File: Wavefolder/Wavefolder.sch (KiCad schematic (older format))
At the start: 43 parts, among them J1 Clock, J2 EuroPower, J3 SSD1306, J4 CV, J5 Gate, Q1 BC547, Q2 BC557, SW1 Reset, U1 TL082, U2 L7805, U3 PIC18F26Q43

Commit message: Wavefolder, will it fits ?
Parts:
- removed C3: 10u, Capacitor_THT:CP_Radial_D8.0mm_P3.80mm, symbol Device:CP
- removed C4: 1u, Capacitor_THT:CP_Radial_D8.0mm_P3.80mm, symbol Device:CP
- removed C5: 100n, Capacitor_THT:C_Disc_D7.0mm_W2.5mm_P5.00mm, symbol Device:C
- removed C6: 10n, Capacitor_THT:C_Disc_D7.0mm_W2.5mm_P5.00mm, symbol Device:C
- removed D1, D2, D4, D5: LED, LED_SMD:LED_1206_3216Metric_Castellated, symbol Device:LED
- removed H3, H4: Mounting_Holes, Kosmo_panel:Kosmo_Panel_Dual_Mounting_Holes, symbol Kosmo:Mounting_Holes
- removed J3: SSD1306, telec:SSD1306_096in_I2C, symbol Connector:Conn_01x05_Female
- removed RV3: R_POT_TRIM, Potentiometer_THT:Potentiometer_Bourns_3299W_Vertical, symbol Device:R_POT_TRIM
- removed SW1: Reset, Button_Switch_THT:SW_PUSH_6mm, symbol Switch:SW_SPST
- removed U2: L7805, Package_TO_SOT_THT:TO-220-3_Horizontal_TabDown, symbol Regulator_Linear:L7805
- removed U3: PIC18F26Q43, Package_SO:SOIC-28W_7.5x17.9mm_P1.27mm, symbol telec:PIC18F26Q43
- added J3: Sig2, telec:JackHole, symbol Connector:AudioJack3_Switch
- added J6: CV2, telec:JackHole, symbol Connector:AudioJack3_Switch
- added Q3, Q5: BC557, Package_TO_SOT_THT:TO-92_Inline_Wide, symbol Transistor_BJT:BC557
- added Q4, Q6: BC547, Package_TO_SOT_THT:TO-92_Inline_Wide, symbol Transistor_BJT:BC547
- added R13, R14: 10k, Resistor_THT:R_Axial_DIN0204_L3.6mm_D1.6mm_P7.62mm_Horizontal, symbol Device:R
- added RV3: 100k, Potentiometer_THT:Potentiometer_Alps_RK09K_Single_Vertical, symbol Device:R_POT
- added U1, U3: TL074, Package_DIP:DIP-14_W7.62mm_LongPads, symbol Amplifier_Operational:TL074
- J1: value Clock -> Sig1
- J4: value CV -> Out1
- J5: value Gate -> Out2
- LOGO1: footprint logo:telec-32 -> logo:telec-8
- R1: value 100k -> 15k
- R11, R12: value 1k -> 15k
- R2, R6: value 10k -> 15k
- R4: value 1k -> 47k; footprint Resistor_SMD:R_1206_3216Metric_Pad1.42x1.75mm_HandSolder -> Resistor_THT:R_Axial_DIN0204_L3.6mm_D1.6mm_P7.62mm_Horizontal
- R5: value 1k -> 15k; footprint Resistor_SMD:R_1206_3216Metric_Pad1.42x1.75mm_HandSolder -> Resistor_THT:R_Axial_DIN0204_L3.6mm_D1.6mm_P7.62mm_Horizontal
- R7: value 1k -> 2k2; footprint Resistor_SMD:R_1206_3216Metric_Pad1.42x1.75mm_HandSolder -> Resistor_THT:R_Axial_DIN0204_L3.6mm_D1.6mm_P7.62mm_Horizontal
- R8: value 1k -> 15K; footprint Resistor_SMD:R_1206_3216Metric_Pad1.42x1.75mm_HandSolder -> Resistor_THT:R_Axial_DIN0204_L3.6mm_D1.6mm_P7.62mm_Horizontal
- R9: value 10k -> 6k8
- RV1: value R_POT_Small -> 100k; footprint Potentiometer_THT:Potentiometer_Bourns_3339P_Vertical -> Potentiometer_THT:Potentiometer_Alps_RK09K_Single_Vertical; symbol Device:R_POT_Small -> Device:R_POT
- RV2: value R_POT -> 100k; footprint Potentiometer_THT:Potentiometer_Piher_T-16L_Single_Vertical_Hole -> Potentiometer_THT:Potentiometer_Alps_RK09K_Single_Vertical
- renumbered U1 to U2
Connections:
- net labels added: CV2, Out1, Sig1, Sig2
- net labels removed: +5V, Rst, SCL, SDA
- wire segments 59 -> 69
- no-connect marks 11 -> 17
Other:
- note added: "This part from Adamski A."
- note added: "This part from organfairy"
- note added: "x -1"
- note added: "x -4.7"
- note added: "x -6.8"
- note removed: "Output buffer"
- moved on the sheet: C1, C2, D3, J1, Q1, Q2, R1, U2A, U2B, U2C

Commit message: Wavefolder layout
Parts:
- removed D6: LED, LED_SMD:LED_1206_3216Metric_ReverseMount_Hole1.8x2.4mm, symbol Device:LED
- removed R10: 1k, Resistor_SMD:R_1206_3216Metric_Pad1.42x1.75mm_HandSolder, symbol Device:R
- added D1, D2, D4: 1N4148, Diode_THT:D_DO-35_SOD27_P7.62mm_Horizontal, symbol Diode:1N4148
- added R15, R16, R26, R27, R28, R29: 100k, Resistor_SMD:R_1206_3216Metric_Pad1.42x1.75mm_HandSolder, symbol Device:R
- added R17, R18, R19, R20, R22: 100k, Resistor_THT:R_Axial_DIN0204_L3.6mm_D1.6mm_P7.62mm_Horizontal, symbol Device:R
- added R21: 100k, Resistor_THT:R_Axial_DIN0204_L3.6mm_D1.6mm_P2.54mm_Vertical, symbol Device:R
- added R23, R24: 15k, Resistor_THT:R_Axial_DIN0204_L3.6mm_D1.6mm_P7.62mm_Horizontal, symbol Device:R
- added R25: 1k, Resistor_SMD:R_1206_3216Metric_Pad1.42x1.75mm_HandSolder, symbol Device:R
- added unit 1 of U1
- added unit 1 of U3
- added unit 4 of U3
- added unit 3 of U3
- added unit 5 of U3
- added U4: TL082, Package_SO:SOIC-8_3.9x4.9mm_P1.27mm, symbol Amplifier_Operational:TL082
- R1, R11, R12, R13, R14, R2, R4, R5, R6, R7, R8, R9: footprint Resistor_THT:R_Axial_DIN0204_L3.6mm_D1.6mm_P7.62mm_Horizontal -> Resistor_THT:R_Axial_DIN0204_L3.6mm_D1.6mm_P2.54mm_Vertical
- U2: footprint Package_DIP:DIP-8_W7.62mm_LongPads -> Package_SO:SOIC-8_3.9x4.9mm_P1.27mm
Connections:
- net +12V: now also RV3.1, R24.2, U3.4 (V+), U4.8 (V+)
- net -12V: now also RV3.3, R23.1, U3.11 (V-), U4.4 (V-)
- net CV2: now also R26.1
- net GND: now also U2.5 (+), U3.3 (+), U4.5 (+)
- net Out1: now also R14.1; no longer R14.2
- net Sig2: now also R15.1
- net at RV1.2: now also U1.3 (+)
- net at D3.1 (K): now also U3.5 (+), D1.1 (K), R23.2
- net ~Sig2: now reaches D3.2 (A)
- net ~Sig2: now also R16.2, R17.1, R18.1, U4.7
- net at J5.T: now also R25.2, U4.2 (-)
- net Offset: now reaches U2.1
- net Offset: now also R19.1, R29.2, U3.10 (+)
- net at U2.2 (-): now also R28.2, R29.1
- net at U2.3 (+): now also RV3.2
- net at U2.6 (-): now also RV2.2, RV2.3, R26.2
- net at U2.7: now also R27.2, R28.1
- net at Q1.2 (B), Q2.2 (B): now also U1.1, U1.2 (-)
- net at R9.1, U1.8: now also R8.1; no longer R8.2
- net at R7.2, U1.9 (-): now also R8.2; no longer R8.1
- net at Q5.1 (C), Q6.1 (C): now also R13.2; no longer R13.1
- net at RV2.1: now also R27.1
- net at U3.6 (-): now also U3.7, D2.1 (K)
- new net: R13.1, R14.2, U1.13 (-)
- new net: R19.2, R22.1, U3.2 (-)
- new net: R18.2, R21.1, U3.13 (-)
- new net: R17.2, R20.1, U3.9 (-)
- new net: R25.1, U4.1
- new net: R15.2, R16.1, U4.6 (-)
- new net Bottom: D1.2 (A), R21.2, U3.14
- new net Out2: D2.2 (A), D4.2 (A), R24.1, U4.3 (+)
- new net Top: D4.1 (K), R20.2, U3.8
- new net ~Offset: R22.2, U3.1, U3.12 (+)
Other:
- note added: "This part is from Adamski A."
- note added: "This part is from organfairy"
- note removed: "Front Panel"
- note removed: "This part from Adamski A."
- note removed: "This part from organfairy"
- moved on the sheet: C1, C2, D3, H1, H2, J1, J2, J3, J4, J5, J6, Q1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

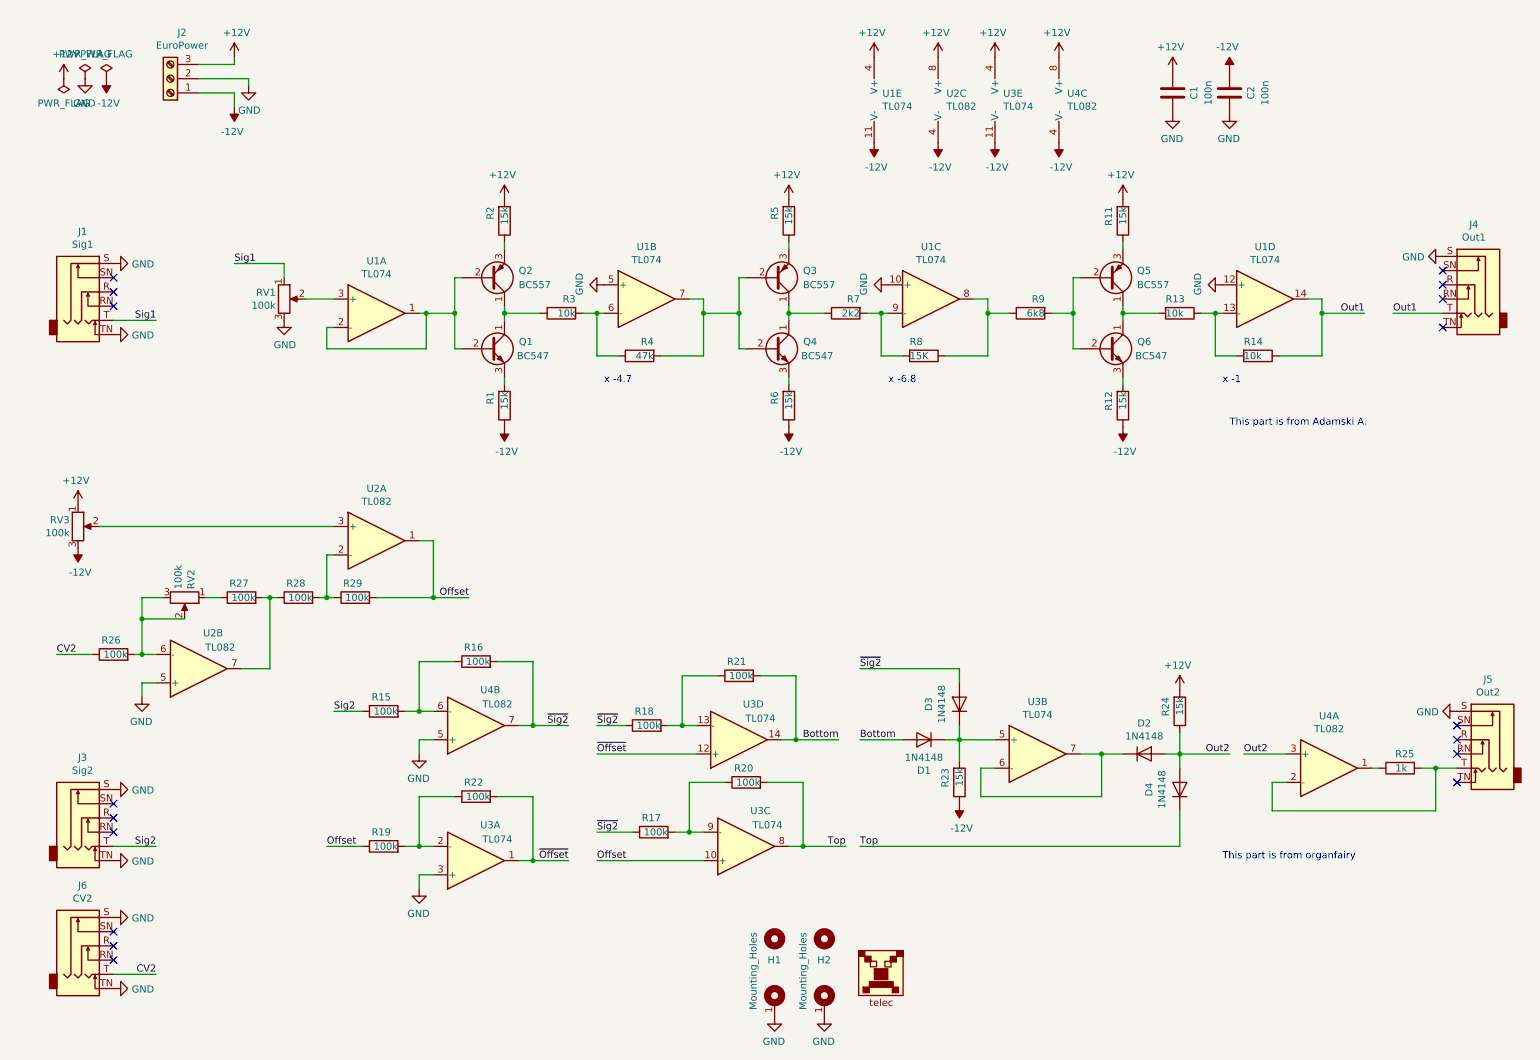
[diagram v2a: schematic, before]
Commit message: Wavefolder design
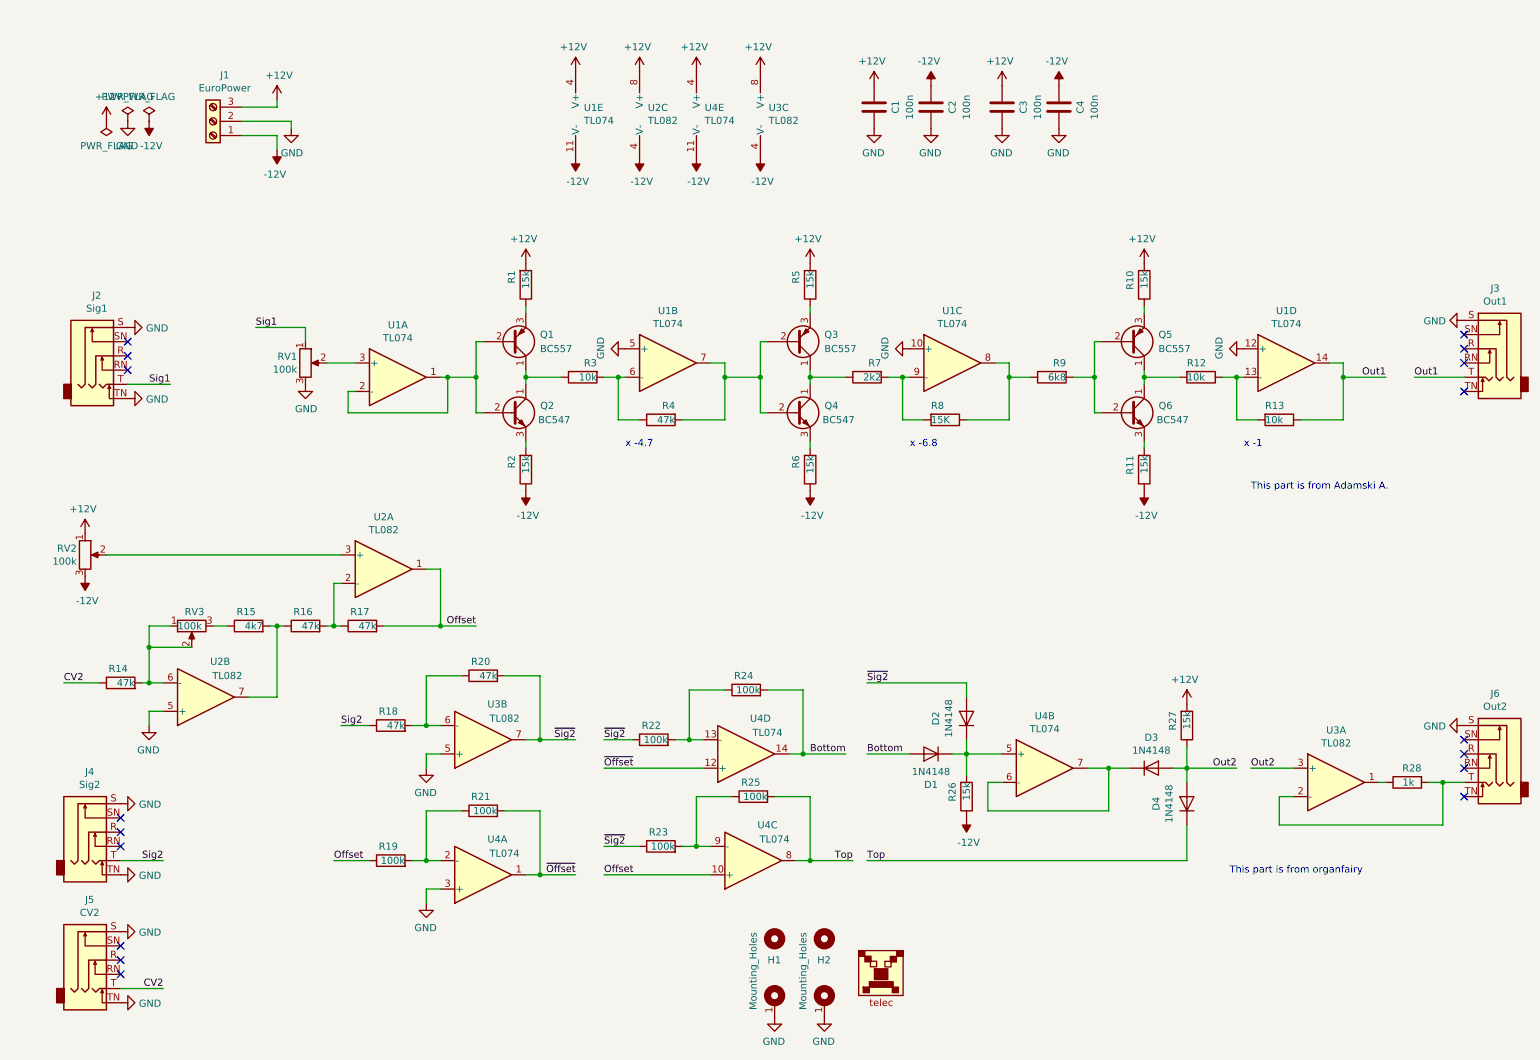
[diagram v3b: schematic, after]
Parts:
- added C3, C4: 100n, Capacitor_SMD:C_1206_3216Metric, symbol Device:C
- C1, C2: footprint Capacitor_THT:C_Disc_D7.0mm_W2.5mm_P5.00mm -> Capacitor_SMD:C_1206_3216Metric
- R14: renamed from R26; value 100k -> 47k
- R15: renamed from R27; value 100k -> 4k7
- R16: renamed from R28; value 100k -> 47k
- R17: renamed from R29; value 100k -> 47k
- R18: renamed from R15; value 100k -> 47k
- R20: renamed from R16; value 100k -> 47k
- renumbered D3 to D2, D2 to D3, J2 to J1, J1 to J2, J4 to J3, J3 to J4, J6 to J5, J5 to J6, Q2 to Q1, Q1 to Q2, R2 to R1, R11 to R10, R12 to R11, R13 to R12, R14 to R13, R1 to R2, R22 to R21, R18 to R22, R17 to R23, R21 to R24, R20 to R25, R23 to R26, R24 to R27, R25 to R28, RV3 to RV2, RV2 to RV3, U4 to U3, U3 to U4
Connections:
- net +12V: now also C3.2
- net -12V: now also C4.2
- net GND: now also C3.1, C4.1
- net at RV3.1: now also R14.2, RV3.2, U2.6 (-); no longer R15.1
- new net: R15.1, RV3.3
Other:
- moved on the sheet: C1, C2, D1, D2, D3, D4, J1, J2, J3, J4, J5, J6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

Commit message: Wavefolder done !
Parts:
- U2, U3: footprint Package_DIP:DIP-8_W7.62mm_LongPads -> Package_SO:SOIC-8_3.9x4.9mm_P1.27mm
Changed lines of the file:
@@
 F 0 "U2" H 4908 1196 50  0000 L CNN
 F 1 "TL082" H 4908 1105 50  0000 L CNN
-F 2 "Package_DIP:DIP-8_W7.62mm_LongPads" H 4950 1150 50  0001 C CNN
+F 2 "Package_SO:SOIC-8_3.9x4.9mm_P1.27mm" H 4950 1150 50  0001 C CNN
 F 3 "http://www.ti.com/lit/ds/symlink/tl081.pdf" H 4950 1150 50  0001 C CNN
 	3    4950 1150
@@
 F 0 "U3" H 5758 1196 50  0000 L CNN
 F 1 "TL082" H 5758 1105 50  0000 L CNN
-F 2 "Package_DIP:DIP-8_W7.62mm_LongPads" H 5800 1150 50  0001 C CNN
+F 2 "Package_SO:SOIC-8_3.9x4.9mm_P1.27mm" H 5800 1150 50  0001 C CNN
 F 3 "http://www.ti.com/lit/ds/symlink/tl081.pdf" H 5800 1150 50  0001 C CNN
 	3    5800 1150

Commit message: Wavefolder done and tested!
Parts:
- added R13.1: 1k, Resistor_THT:R_Axial_DIN0204_L3.6mm_D1.6mm_P2.54mm_Vertical, symbol Device:R
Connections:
- net Out1: now also R13.1.1; no longer J3.T
- new net: J3.T, R13.1.2
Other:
- moved on the sheet: Q1, Q2, Q3, Q4, Q5, Q6, R1, R10, R11, R12, R13, R2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

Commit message: updated footprints on Wavefolder
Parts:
- J2, J3, J4, J5, J6: footprint telec:JackHole -> telec:Jack_Hole_Square; symbol Connector:AudioJack3_Switch -> Connector:AudioJack3_SwitchTR
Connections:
- no-connect marks 17 -> 12
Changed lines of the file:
@@
 $EndComp
 $Comp
-L Connector:AudioJack3_Switch J2
+L Connector:AudioJack3_SwitchTR J2
 U 1 1 5F0BD040
 P 1050 2850
 F 0 "J2" H 1032 3275 50  0000 C CNN
 F 1 "Sig1" H 1032 3184 50  0000 C CNN
-F 2 "telec:JackHole" H 1050 2850 50  0001 C CNN
+F 2 "telec:Jack_Hole_Square" H 1050 2850 50  0001 C CNN
 F 3 "~" H 1050 2850 50  0001 C CNN
 	1    1050 2850
@@
 	2300 1300 2300 1400
 $Comp
-L Connector:AudioJack3_Switch J6
+L Connector:AudioJack3_SwitchTR J6
 U 1 1 5F41F070
 P 10850 5650
 F 0 "J6" H 10832 6075 50  0000 C CNN
 F 1 "Out2" H 10832 5984 50  0000 C CNN
-F 2 "telec:JackHole" H 10850 5650 50  0001 C CNN
+F 2 "telec:Jack_Hole_Square" H 10850 5650 50  0001 C CNN
 F 3 "~" H 10850 5650 50  0001 C CNN
 	1    10850 5650
@@
 $EndComp
 $Comp
-L Connector:AudioJack3_Switch J3
+L Connector:AudioJack3_SwitchTR J3
 U 1 1 5F4208DD
 P 10850 2800
 F 0 "J3" H 10832 3225 50  0000 C CNN
 F 1 "Out1" H 10832 3134 50  0000 C CNN
-F 2 "telec:JackHole" H 10850 2800 50  0001 C CNN
+F 2 "telec:Jack_Hole_Square" H 10850 2800 50  0001 C CNN
 F 3 "~" H 10850 2800 50  0001 C CNN
 	1    10850 2800
@@
 NoConn ~ 10650 5750
 NoConn ~ 10650 5650
-NoConn ~ 10650 5550
 NoConn ~ 10650 5950
 $Comp
 L power:GND #PWR033
 U 1 1 5F62E5EC
-P 10650 5450
-F 0 "#PWR033" H 10650 5200 50  0001 C CNN
-F 1 "GND" V 10655 5322 50  0000 R CNN
-F 2 "" H 10650 5450 50  0001 C CNN
-F 3 "" H 10650 5450 50  0001 C CNN
-	1    10650 5450
+P 10650 5550
+F 0 "#PWR033" H 10650 5300 50  0001 C CNN
+F 1 "GND" V 10655 5422 50  0000 R CNN
+F 2 "" H 10650 5550 50  0001 C CNN
+F 3 "" H 10650 5550 50  0001 C CNN
+	1    10650 5550
 	0    1    1    0
 $EndComp
 NoConn ~ 10650 2900
 NoConn ~ 10650 2800
-NoConn ~ 10650 2700
 NoConn ~ 10650 3100
 $Comp
 L power:GND #PWR019
 U 1 1 5F62EF49
-P 10650 2600
-F 0 "#PWR019" H 10650 2350 50  0001 C CNN
-F 1 "GND" V 10655 2472 50  0000 R CNN
-F 2 "" H 10650 2600 50  0001 C CNN
-F 3 "" H 10650 2600 50  0001 C CNN
-	1    10650 2600
+P 10650 2700
+F 0 "#PWR019" H 10650 2450 50  0001 C CNN
+F 1 "GND" V 10655 2572 50  0000 R CNN
+F 2 "" H 10650 2700 50  0001 C CNN
+F 3 "" H 10650 2700 50  0001 C CNN
+	1    10650 2700
 	0    1    1    0
 $EndComp
 NoConn ~ 1250 2950
 NoConn ~ 1250 2850
-NoConn ~ 1250 2750
 $Comp
 L power:GND #PWR07
 U 1 1 5F63005B
-P 1250 2650
-F 0 "#PWR07" H 1250 2400 50  0001 C CNN
-F 1 "GND" V 1255 2522 50  0000 R CNN
-F 2 "" H 1250 2650 50  0001 C CNN
-F 3 "" H 1250 2650 50  0001 C CNN
-	1    1250 2650
+P 1250 2750
+F 0 "#PWR07" H 1250 2500 50  0001 C CNN
+F 1 "GND" V 1255 2622 50  0000 R CNN
+F 2 "" H 1250 2750 50  0001 C CNN
+F 3 "" H 1250 2750 50  0001 C CNN
+	1    1250 2750
 	0    -1   1    0
 $EndComp
@@
 Sig1
 $Comp
-L Connector:AudioJack3_Switch J4
+L Connector:AudioJack3_SwitchTR J4
 U 1 1 6449AD27
 P 1000 6200
 F 0 "J4" H 982 6625 50  0000 C CNN
 F 1 "Sig2" H 982 6534 50  0000 C CNN
-F 2 "telec:JackHole" H 1000 6200 50  0001 C CNN
+F 2 "telec:Jack_Hole_Square" H 1000 6200 50  0001 C CNN
 F 3 "~" H 1000 6200 50  0001 C CNN
 	1    1000 6200
@@
 NoConn ~ 1200 6300
 NoConn ~ 1200 6200
-NoConn ~ 1200 6100
 $Comp
 L power:GND #PWR022
 U 1 1 6449AD30
-P 1200 6000
-F 0 "#PWR022" H 1200 5750 50  0001 C CNN
-F 1 "GND" V 1205 5872 50  0000 R CNN
-F 2 "" H 1200 6000 50  0001 C CNN
-F 3 "" H 1200 6000 50  0001 C CNN
-	1    1200 6000
+P 1200 6100
+F 0 "#PWR022" H 1200 5850 50  0001 C CNN
+F 1 "GND" V 1205 5972 50  0000 R CNN
+F 2 "" H 1200 6100 50  0001 C CNN
+F 3 "" H 1200 6100 50  0001 C CNN
+	1    1200 6100
 	0    -1   1    0
 $EndComp
@@
 Sig2
 $Comp
-L Connector:AudioJack3_Switch J5
+L Connector:AudioJack3_SwitchTR J5
 U 1 1 6449C304
 P 1000 7100
 F 0 "J5" H 982 7525 50  0000 C CNN
 F 1 "CV2" H 982 7434 50  0000 C CNN
-F 2 "telec:JackHole" H 1000 7100 50  0001 C CNN
+F 2 "telec:Jack_Hole_Square" H 1000 7100 50  0001 C CNN
 F 3 "~" H 1000 7100 50  0001 C CNN
 	1    1000 7100
@@
 NoConn ~ 1200 7200
 NoConn ~ 1200 7100
-NoConn ~ 1200 7000
 $Comp
 L power:GND #PWR024
 U 1 1 6449C30D
-P 1200 6900
-F 0 "#PWR024" H 1200 6650 50  0001 C CNN
-F 1 "GND" V 1205 6772 50  0000 R CNN
-F 2 "" H 1200 6900 50  0001 C CNN
-F 3 "" H 1200 6900 50  0001 C CNN
-	1    1200 6900
+P 1200 7000
+F 0 "#PWR024" H 1200 6750 50  0001 C CNN
+F 1 "GND" V 1205 6872 50  0000 R CNN
+F 2 "" H 1200 7000 50  0001 C CNN
+F 3 "" H 1200 7000 50  0001 C CNN
+	1    1200 7000
 	0    -1   1    0
 $EndComp
